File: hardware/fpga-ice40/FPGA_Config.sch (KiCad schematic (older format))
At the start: 8 parts, among them U1 iCE40HX4K-TQ144, U10 SN74LVC1G08DBVR, X1 ECS-2520MV-xxx-xx

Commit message: Component selection by MPN and routing cleanup
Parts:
- C44: MPN (none) -> CL10B104KB8NNNC
- U1: MPN (none) -> iCE40HX4K-TQ144; manf# iCE40HX4K-TQ144 -> (none)
- U10: value SN74LVC1G08DBVR -> MC74HC1G08DTT1G; MPN (none) -> MC74HC1G08DTT1G
- X1: value ECS-2520MV-xxx-xx -> 50MHz; MPN (none) -> ECS-2520MV-500-BN-TR
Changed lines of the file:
@@
 F 2 "Package_QFP:TQFP-144_20x20mm_P0.5mm" H 4300 3500 60  0001 L CNN
 F 3 "https://www.mouser.com/datasheet/2/225/FPGA-DS-02029-3-5-iCE40-LP-HX-Family-Data-Sheet-1022803.pdf" H 4300 3300 60  0001 L CNN
-F 4 "iCE40HX4K-TQ144" H 4300 3400 60  0001 L CNN "manf#"
+F 4 "" H 4300 3400 60  0001 L CNN "manf#"
+F 5 "iCE40HX4K-TQ144" H 4100 3450 50  0001 C CNN "MPN"
 	5    4100 3450
 	-1   0    0    -1
@@
 F 2 "Package_QFP:TQFP-144_20x20mm_P0.5mm" H 4300 4850 60  0001 L CNN
 F 3 "https://www.mouser.com/datasheet/2/225/FPGA-DS-02029-3-5-iCE40-LP-HX-Family-Data-Sheet-1022803.pdf" H 4300 4650 60  0001 L CNN
-F 4 "iCE40HX4K-TQ144" H 4300 4750 60  0001 L CNN "manf#"
+F 4 "" H 4300 4750 60  0001 L CNN "manf#"
+F 5 "iCE40HX4K-TQ144" H 4100 4800 50  0001 C CNN "MPN"
 	8    4100 4800
 	-1   0    0    -1
@@
 AR Path="/5F5B53E5/5F5C1BBC" Ref="X1"  Part="1"
 F 0 "X1" H 6450 5300 50  0000 L CNN
-F 1 "ECS-2520MV-xxx-xx" H 6850 5300 50  0000 L CNN
+F 1 "50MHz" H 6850 5300 50  0000 L CNN
 F 2 "ng_time:Oscillator_2.5x2.0" H 7200 4700 50  0001 C CNN
 F 3 "https://www.ecsxtal.com/store/pdf/ECS-2520MV.pdf" H 6575 5175 50  0001 C CNN
+F 4 "ECS-2520MV-500-BN-TR" H 6750 5050 50  0001 C CNN "MPN"
 	1    6750 5050
 	1    0    0    -1
@@
 F 2 "Capacitor_SMD:C_0603_1608Metric" H 6088 5050 50  0001 C CNN
 F 3 "~" H 6050 5200 50  0001 C CNN
+F 4 "CL10B104KB8NNNC" H 6050 5200 50  0001 C CNN "MPN"
 	1    6050 5200
 	1    0    0    -1
@@
 P 6950 3750
 F 0 "U10" H 7000 4000 50  0000 L CNN
-F 1 "SN74LVC1G08DBVR" H 7000 3900 50  0000 L CNN
+F 1 "MC74HC1G08DTT1G" H 7000 3900 50  0000 L CNN
 F 2 "Package_TO_SOT_SMD:SOT-23-5" H 6950 3750 50  0001 C CNN
 F 3 "http://www.ti.com/lit/sg/scyt129e/scyt129e.pdf" H 6950 3750 50  0001 C CNN
+F 4 "MC74HC1G08DTT1G" H 6950 3750 50  0001 C CNN "MPN"
 	1    6950 3750
 	1    0    0    -1

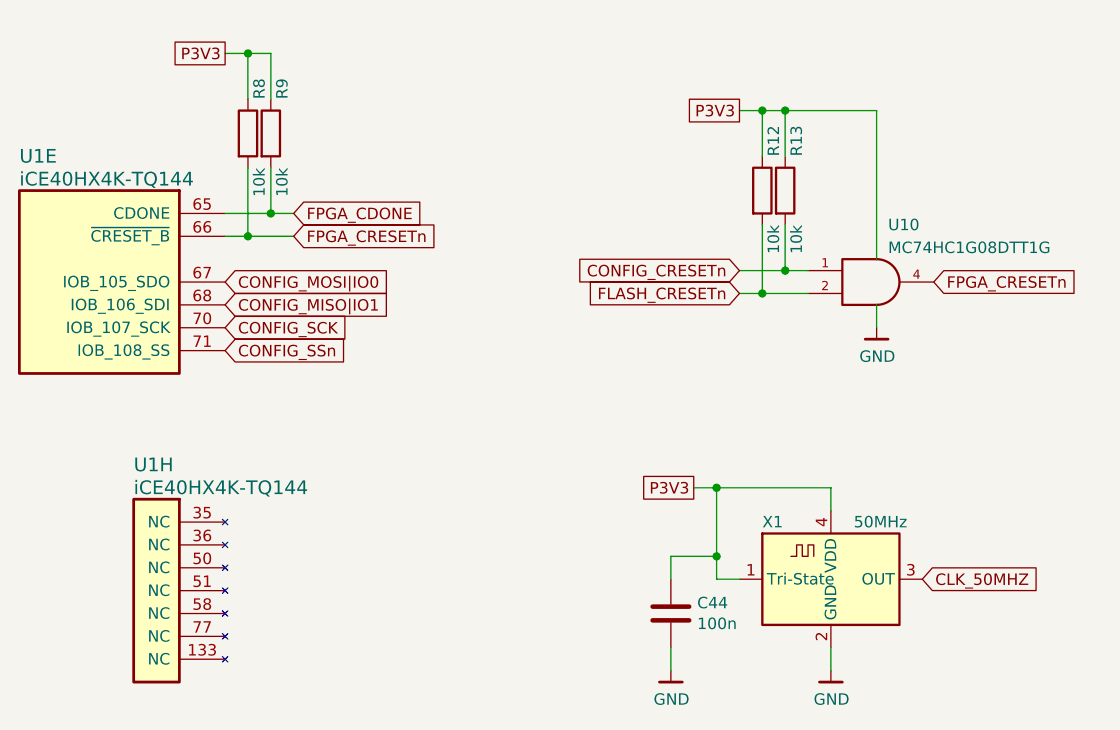
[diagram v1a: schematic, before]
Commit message: Simplify FPGA reset logic layout with resistor array
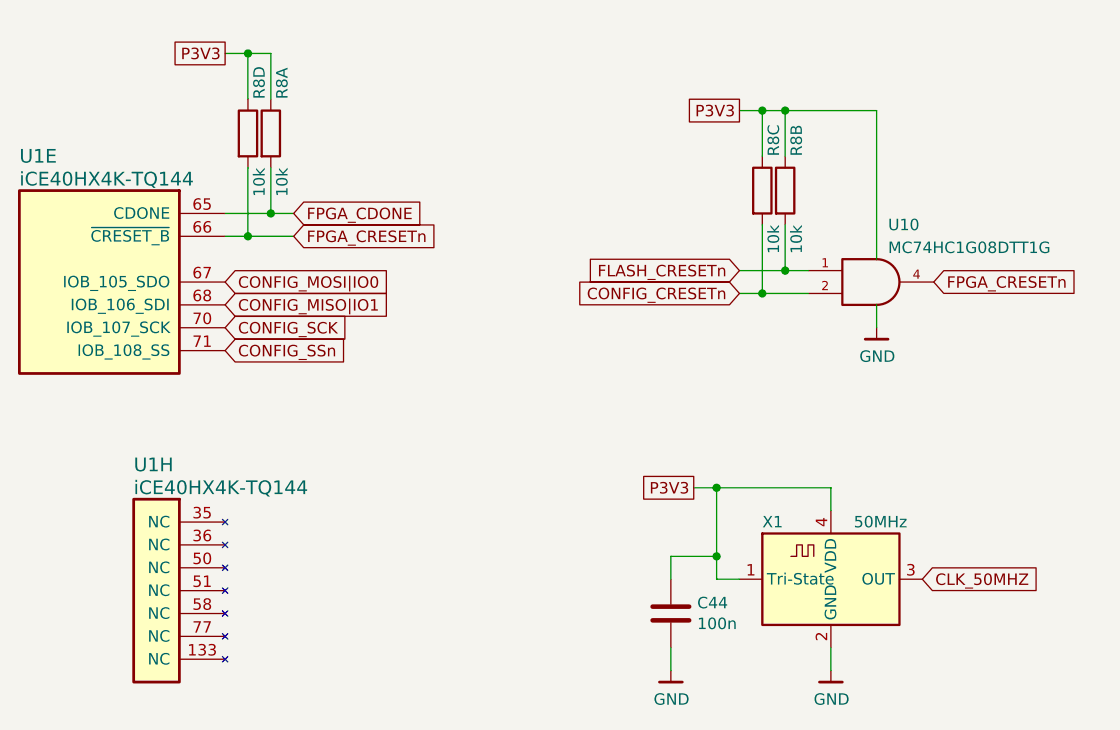
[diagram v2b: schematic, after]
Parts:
- removed R12, R13, R8, R9: 10k, Resistor_SMD:R_0603_1608Metric, symbol Device:R
- added R8: 10k, Resistor_SMD:R_Array_Convex_4x0603, symbol Device:R_Pack04_Split
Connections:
- net CONFIG_CRESETn: now also U10.2, R8.3; no longer U10.1
- net FLASH_CRESETn: now also U10.1, R8.2; no longer U10.2
- net FPGA_CDONE: now also R8.1
- net FPGA_CRESETn: now also R8.4
- net VCC: now also R8.5, R8.6, R8.7, R8.8
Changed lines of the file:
@@
 Text GLabel 4400 3550 2    50   Input ~ 0
 FPGA_CRESETn
-Wire Wire Line
-	4100 3550 4200 3550
-Wire Wire Line
-	4200 3250 4200 3550
-Connection ~ 4200 3550
-Wire Wire Line
-	4100 3450 4300 3450
-$Comp
-L Device:R R?
-U 1 1 5F5C1BA6
-P 4200 3100
-AR Path="/5F5C1BA6" Ref="R?"  Part="1"
-AR Path="/5F5B53E5/5F5C1BA6" Ref="R8"  Part="1"
-F 0 "R8" V 4250 3250 50  0000 L CNN
-F 1 "10k" V 4250 2950 50  0000 R CNN
-F 2 "Resistor_SMD:R_0603_1608Metric" V 4130 3100 50  0001 C CNN
-F 3 "~" H 4200 3100 50  0001 C CNN
-	1    4200 3100
-	1    0    0    -1
-$EndComp
-Wire Wire Line
-	4200 3550 4400 3550
-Wire Wire Line
-	4300 3450 4300 3250
-Connection ~ 4300 3450
-Wire Wire Line
-	4300 3450 4400 3450
-Wire Wire Line
-	4200 2950 4200 2750
-Wire Wire Line
-	4200 2750 4300 2750
-Wire Wire Line
-	4300 2750 4300 2950
-$Comp
-L Device:R R?
-U 1 1 5F5C1BB3
-P 4300 3100
-AR Path="/5F5C1BB3" Ref="R?"  Part="1"
-AR Path="/5F5B53E5/5F5C1BB3" Ref="R9"  Part="1"
-F 0 "R9" V 4350 3250 50  0000 L CNN
-F 1 "10k" V 4350 2950 50  0000 R CNN
-F 2 "Resistor_SMD:R_0603_1608Metric" V 4230 3100 50  0001 C CNN
-F 3 "~" H 4300 3100 50  0001 C CNN
-	1    4300 3100
-	1    0    0    -1
-$EndComp
 Text GLabel 4100 2750 0    50   UnSpc ~ 0
 P3V3
-Wire Wire Line
-	4100 2750 4200 2750
-Connection ~ 4200 2750
 $Comp
 L Oscillator:ECS-2520MV-xxx-xx X?
@@
 Wire Wire Line
 	6950 3650 6950 3000
-Wire Wire Line
-	6950 3000 6550 3000
 $Comp
 L ng_power:GND #PWR035
@@
 Wire Wire Line
 	6450 3500 6450 3800
-$Comp
-L Device:R R?
-U 1 1 5EFB670F
-P 6450 3350
-AR Path="/5EFB670F" Ref="R?"  Part="1"
-AR Path="/5F5B53E5/5EFB670F" Ref="R12"  Part="1"
-F 0 "R12" V 6500 3500 50  0000 L CNN
-F 1 "10k" V 6500 3200 50  0000 R CNN
-F 2 "Resistor_SMD:R_0603_1608Metric" V 6380 3350 50  0001 C CNN
-F 3 "~" H 6450 3350 50  0001 C CNN
-	1    6450 3350
-	1    0    0    -1
-$EndComp
 Wire Wire Line
 	6550 3700 6550 3500
-Wire Wire Line
-	6450 3200 6450 3000
-Wire Wire Line
-	6450 3000 6550 3000
-Wire Wire Line
-	6550 3000 6550 3200
-$Comp
-L Device:R R?
-U 1 1 5EFB671D
-P 6550 3350
-AR Path="/5EFB671D" Ref="R?"  Part="1"
-AR Path="/5F5B53E5/5EFB671D" Ref="R13"  Part="1"
-F 0 "R13" V 6600 3500 50  0000 L CNN
-F 1 "10k" V 6600 3200 50  0000 R CNN
-F 2 "Resistor_SMD:R_0603_1608Metric" V 6480 3350 50  0001 C CNN
-F 3 "~" H 6550 3350 50  0001 C CNN
-	1    6550 3350
-	1    0    0    -1
-$EndComp
 Text GLabel 6350 3000 0    50   UnSpc ~ 0
 P3V3
 Wire Wire Line
-	6350 3000 6450 3000
-Connection ~ 6450 3000
-Connection ~ 6550 3000
-Wire Wire Line
 	6650 3700 6550 3700
 Connection ~ 6550 3700
@@
 Wire Wire Line
 	6450 3800 6350 3800
+Text GLabel 6350 3700 0    50   Input ~ 0
+FLASH_CRESETn
 Text GLabel 6350 3800 0    50   Input ~ 0
-FLASH_CRESETn
-Text GLabel 6350 3700 0    50   Input ~ 0
 CONFIG_CRESETn
+$Comp
+L Device:R_Pack04_Split R?
+U 4 1 5EFC6F2A
+P 4200 3100
+AR Path="/5EFC6F2A" Ref="R?"  Part="1"
+AR Path="/5F90C399/5EFC6F2A" Ref="R?"  Part="1"
+AR Path="/5F5B53E5/5EFC6F2A" Ref="R8"  Part="4"
+F 0 "R8" V 4250 3250 50  0000 L CNN
+F 1 "10k" V 4250 2950 50  0000 R CNN
+F 2 "Resistor_SMD:R_Array_Convex_4x0603" V 4130 3100 50  0001 C CNN
+F 3 "~" H 4200 3100 50  0001 C CNN
+	4    4200 3100
+	1    0    0    -1
+$EndComp
+$Comp
+L Device:R_Pack04_Split R?
+U 3 1 5EFC6F23
+P 6450 3350
+AR Path="/5EFC6F23" Ref="R?"  Part="2"
+AR Path="/5F90C399/5EFC6F23" Ref="R?"  Part="2"
+AR Path="/5F5B53E5/5EFC6F23" Ref="R8"  Part="3"
+F 0 "R8" V 6500 3500 50  0000 L CNN
+F 1 "10k" V 6500 3200 50  0000 R CNN
+F 2 "Resistor_SMD:R_Array_Convex_4x0603" V 6380 3350 50  0001 C CNN
+F 3 "~" H 6450 3350 50  0001 C CNN
+	3    6450 3350
+	1    0    0    -1
+$EndComp
+$Comp
+L Device:R_Pack04_Split R?
+U 2 1 5EFC6F1C
+P 6550 3350
+AR Path="/5EFC6F1C" Ref="R?"  Part="3"
+AR Path="/5F90C399/5EFC6F1C" Ref="R?"  Part="3"
+AR Path="/5F5B53E5/5EFC6F1C" Ref="R8"  Part="2"
+F 0 "R8" V 6600 3500 50  0000 L CNN
+F 1 "10k" V 6600 3200 50  0000 R CNN
+F 2 "Resistor_SMD:R_Array_Convex_4x0603" V 6480 3350 50  0001 C CNN
+F 3 "~" H 6550 3350 50  0001 C CNN
+	2    6550 3350
+	1    0    0    -1
+$EndComp
+$Comp
+L Device:R_Pack04_Split R?
+U 1 1 5EFC6F15
+P 4300 3100
+AR Path="/5EFC6F15" Ref="R?"  Part="4"
+AR Path="/5F90C399/5EFC6F15" Ref="R?"  Part="4"
+AR Path="/5F5B53E5/5EFC6F15" Ref="R8"  Part="1"
+F 0 "R8" V 4350 3250 50  0000 L CNN
+F 1 "10k" V 4350 2950 50  0000 R CNN
+F 2 "Resistor_SMD:R_Array_Convex_4x0603" V 4230 3100 50  0001 C CNN
+F 3 "~" H 4300 3100 50  0001 C CNN
+	1    4300 3100
+	1    0    0    -1
+$EndComp
+Connection ~ 4300 3450
+Wire Wire Line
+	4300 3450 4400 3450
+Wire Wire Line
+	4100 3450 4300 3450
+Connection ~ 4200 3550
+Wire Wire Line
+	4200 3550 4400 3550
+Wire Wire Line
+	4100 3550 4200 3550
+Wire Wire Line
+	4300 3450 4300 3250
+Wire Wire Line
+	4200 3250 4200 3550
+Wire Wire Line
+	6350 3000 6450 3000
+Wire Wire Line
+	6550 3200 6550 3000
+Connection ~ 6550 3000
+Wire Wire Line
+	6550 3000 6950 3000
+Wire Wire Line
+	4200 2950 4200 2750
+Wire Wire Line
+	4300 2950 4300 2750
+Wire Wire Line
+	4100 2750 4200 2750
+Connection ~ 4200 2750
+Wire Wire Line
+	4200 2750 4300 2750
+Wire Wire Line
+	6450 3200 6450 3000
+Connection ~ 6450 3000
+Wire Wire Line
+	6450 3000 6550 3000
 $EndSCHEMATC

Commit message: Complete component selection by MPN
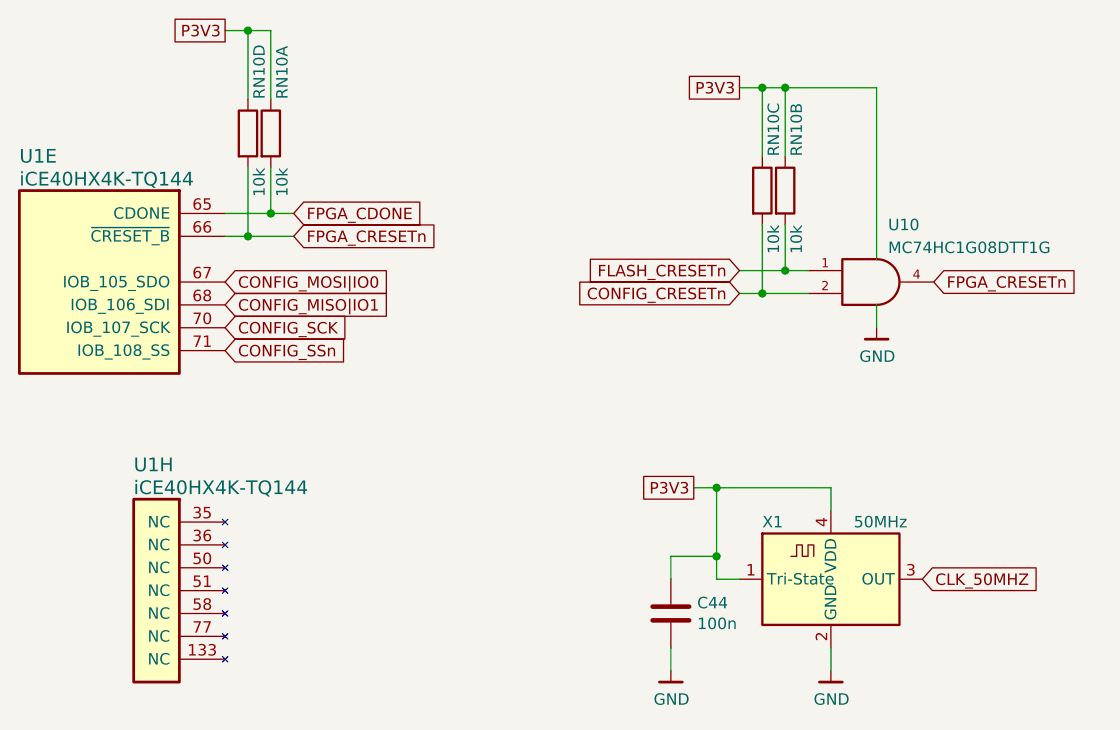
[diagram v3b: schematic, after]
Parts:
- RN10: renamed from R8; MPN (none) -> YC164-JR-0710KL
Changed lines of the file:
@@
 Text GLabel 4400 3550 2    50   Input ~ 0
 FPGA_CRESETn
-Text GLabel 4100 2750 0    50   UnSpc ~ 0
+Text GLabel 4100 2650 0    50   UnSpc ~ 0
 P3V3
 $Comp
@@
 	6950 3850 6950 3950
 Wire Wire Line
-	6950 3650 6950 3000
+	6950 3650 6950 2900
 $Comp
 L ng_power:GND #PWR035
@@
 Wire Wire Line
 	6550 3700 6550 3500
-Text GLabel 6350 3000 0    50   UnSpc ~ 0
+Text GLabel 6350 2900 0    50   UnSpc ~ 0
 P3V3
 Wire Wire Line
@@
 AR Path="/5EFC6F2A" Ref="R?"  Part="1"
 AR Path="/5F90C399/5EFC6F2A" Ref="R?"  Part="1"
-AR Path="/5F5B53E5/5EFC6F2A" Ref="R8"  Part="4"
-F 0 "R8" V 4250 3250 50  0000 L CNN
+AR Path="/5F5B53E5/5EFC6F2A" Ref="RN10"  Part="4"
+F 0 "RN10" V 4250 3250 50  0000 L CNN
 F 1 "10k" V 4250 2950 50  0000 R CNN
 F 2 "Resistor_SMD:R_Array_Convex_4x0603" V 4130 3100 50  0001 C CNN
 F 3 "~" H 4200 3100 50  0001 C CNN
+F 4 "YC164-JR-0710KL" H 4200 3100 50  0001 C CNN "MPN"
 	4    4200 3100
 	1    0    0    -1
@@
 AR Path="/5EFC6F23" Ref="R?"  Part="2"
 AR Path="/5F90C399/5EFC6F23" Ref="R?"  Part="2"
-AR Path="/5F5B53E5/5EFC6F23" Ref="R8"  Part="3"
-F 0 "R8" V 6500 3500 50  0000 L CNN
+AR Path="/5F5B53E5/5EFC6F23" Ref="RN10"  Part="3"
+F 0 "RN10" V 6500 3500 50  0000 L CNN
 F 1 "10k" V 6500 3200 50  0000 R CNN
 F 2 "Resistor_SMD:R_Array_Convex_4x0603" V 6380 3350 50  0001 C CNN
 F 3 "~" H 6450 3350 50  0001 C CNN
+F 4 "YC164-JR-0710KL" H 6450 3350 50  0001 C CNN "MPN"
 	3    6450 3350
 	1    0    0    -1
@@
 AR Path="/5EFC6F1C" Ref="R?"  Part="3"
 AR Path="/5F90C399/5EFC6F1C" Ref="R?"  Part="3"
-AR Path="/5F5B53E5/5EFC6F1C" Ref="R8"  Part="2"
-F 0 "R8" V 6600 3500 50  0000 L CNN
+AR Path="/5F5B53E5/5EFC6F1C" Ref="RN10"  Part="2"
+F 0 "RN10" V 6600 3500 50  0000 L CNN
 F 1 "10k" V 6600 3200 50  0000 R CNN
 F 2 "Resistor_SMD:R_Array_Convex_4x0603" V 6480 3350 50  0001 C CNN
 F 3 "~" H 6550 3350 50  0001 C CNN
+F 4 "YC164-JR-0710KL" H 6550 3350 50  0001 C CNN "MPN"
 	2    6550 3350
 	1    0    0    -1
@@
 AR Path="/5EFC6F15" Ref="R?"  Part="4"
 AR Path="/5F90C399/5EFC6F15" Ref="R?"  Part="4"
-AR Path="/5F5B53E5/5EFC6F15" Ref="R8"  Part="1"
-F 0 "R8" V 4350 3250 50  0000 L CNN
+AR Path="/5F5B53E5/5EFC6F15" Ref="RN10"  Part="1"
+F 0 "RN10" V 4350 3250 50  0000 L CNN
 F 1 "10k" V 4350 2950 50  0000 R CNN
 F 2 "Resistor_SMD:R_Array_Convex_4x0603" V 4230 3100 50  0001 C CNN
 F 3 "~" H 4300 3100 50  0001 C CNN
+F 4 "YC164-JR-0710KL" H 4300 3100 50  0001 C CNN "MPN"
 	1    4300 3100
 	1    0    0    -1
@@
 	4200 3250 4200 3550
 Wire Wire Line
-	6350 3000 6450 3000
-Wire Wire Line
-	6550 3200 6550 3000
-Connection ~ 6550 3000
-Wire Wire Line
-	6550 3000 6950 3000
-Wire Wire Line
-	4200 2950 4200 2750
-Wire Wire Line
-	4300 2950 4300 2750
-Wire Wire Line
-	4100 2750 4200 2750
-Connection ~ 4200 2750
-Wire Wire Line
-	4200 2750 4300 2750
-Wire Wire Line
-	6450 3200 6450 3000
-Connection ~ 6450 3000
-Wire Wire Line
-	6450 3000 6550 3000
+	6350 2900 6450 2900
+Wire Wire Line
+	6550 3200 6550 2900
+Connection ~ 6550 2900
+Wire Wire Line
+	6550 2900 6950 2900
+Wire Wire Line
+	4200 2950 4200 2650
+Wire Wire Line
+	4300 2950 4300 2650
+Wire Wire Line
+	4100 2650 4200 2650
+Connection ~ 4200 2650
+Wire Wire Line
+	4200 2650 4300 2650
+Wire Wire Line
+	6450 3200 6450 2900
+Connection ~ 6450 2900
+Wire Wire Line
+	6450 2900 6550 2900
 $EndSCHEMATC

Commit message: Completed verification of all pins for all symbols
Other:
- moved on the sheet: C44
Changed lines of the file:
@@
 F 1 "50MHz" H 6850 5300 50  0000 L CNN
 F 2 "ng_time:Oscillator_2.5x2.0" H 7200 4700 50  0001 C CNN
-F 3 "https://www.ecsxtal.com/store/pdf/ECS-2520MV.pdf" H 6575 5175 50  0001 C CNN
+F 3 "https://ecsxtal.com/store/pdf/ECS-2520MV.pdf" H 6575 5175 50  0001 C CNN
 F 4 "ECS-2520MV-500-BN-TR" H 6750 5050 50  0001 C CNN "MPN"
 	1    6750 5050
@@
 	1    0    0    -1
 $EndComp
-Text GLabel 6150 4650 0    50   UnSpc ~ 0
+Text GLabel 5950 4650 0    50   UnSpc ~ 0
 P3V3
 Wire Wire Line
 	6350 5050 6250 5050
 Wire Wire Line
-	6250 5050 6250 4950
-Wire Wire Line
 	6250 4650 6750 4650
 Wire Wire Line
 	6750 4650 6750 4750
-Wire Wire Line
-	6150 4650 6250 4650
 Wire Wire Line
 	6750 5450 6750 5350
@@
 CLK_50MHZ
 $Comp
-L Device:C C?
-U 1 1 5F5C1BD0
-P 6050 5200
-AR Path="/5F5C1BD0" Ref="C?"  Part="1"
-AR Path="/5F5B53E5/5F5C1BD0" Ref="C44"  Part="1"
-F 0 "C44" H 6165 5246 50  0000 L CNN
-F 1 "100n" H 6165 5155 50  0000 L CNN
-F 2 "Capacitor_SMD:C_0603_1608Metric" H 6088 5050 50  0001 C CNN
-F 3 "~" H 6050 5200 50  0001 C CNN
-F 4 "CL10B104KB8NNNC" H 6050 5200 50  0001 C CNN "MPN"
-	1    6050 5200
-	1    0    0    -1
-$EndComp
-$Comp
 L ng_power:GND #PWR?
 U 1 1 5F5C1BD6
-P 6050 5450
+P 6050 5150
 AR Path="/5F5C1BD6" Ref="#PWR?"  Part="1"
 AR Path="/5F5B53E5/5F5C1BD6" Ref="#PWR031"  Part="1"
-F 0 "#PWR031" H 6050 5200 50  0001 C CNN
-F 1 "GND" H 6053 5324 50  0000 C CNN
-F 2 "" H 5950 5100 50  0001 C CNN
-F 3 "" H 6050 5450 50  0001 C CNN
-	1    6050 5450
-	1    0    0    -1
-$EndComp
-Wire Wire Line
-	6050 5450 6050 5350
-Wire Wire Line
-	6050 5050 6050 4950
-Wire Wire Line
-	6050 4950 6250 4950
-Connection ~ 6250 4950
-Wire Wire Line
-	6250 4950 6250 4650
+F 0 "#PWR031" H 6050 4900 50  0001 C CNN
+F 1 "GND" H 6053 5024 50  0000 C CNN
+F 2 "" H 5950 4800 50  0001 C CNN
+F 3 "" H 6050 5150 50  0001 C CNN
+	1    6050 5150
+	1    0    0    -1
+$EndComp
+Wire Wire Line
+	6050 5150 6050 5050
 Connection ~ 6250 4650
 $Comp
@@
 F 1 "MC74HC1G08DTT1G" H 7000 3900 50  0000 L CNN
 F 2 "Package_TO_SOT_SMD:SOT-23-5" H 6950 3750 50  0001 C CNN
-F 3 "http://www.ti.com/lit/sg/scyt129e/scyt129e.pdf" H 6950 3750 50  0001 C CNN
+F 3 "https://www.onsemi.com/pub/Collateral/MC74HC1G08-D.PDF" H 6950 3750 50  0001 C CNN
 F 4 "MC74HC1G08DTT1G" H 6950 3750 50  0001 C CNN "MPN"
 	1    6950 3750
@@
 Wire Wire Line
 	6450 2900 6550 2900
+Wire Wire Line
+	6250 4650 6250 5050
+Wire Wire Line
+	5950 4650 6050 4650
+Wire Wire Line
+	6050 4750 6050 4650
+Connection ~ 6050 4650
+Wire Wire Line
+	6050 4650 6250 4650
+$Comp
+L Device:C C?
+U 1 1 5F5C1BD0
+P 6050 4900
+AR Path="/5F5C1BD0" Ref="C?"  Part="1"
+AR Path="/5F5B53E5/5F5C1BD0" Ref="C44"  Part="1"
+F 0 "C44" H 5950 4950 50  0000 R CNN
+F 1 "100n" H 5950 4850 50  0000 R CNN
+F 2 "Capacitor_SMD:C_0603_1608Metric" H 6088 4750 50  0001 C CNN
+F 3 "~" H 6050 4900 50  0001 C CNN
+F 4 "CL10B104KB8NNNC" H 6050 4900 50  0001 C CNN "MPN"
+	1    6050 4900
+	1    0    0    -1
+$EndComp
 $EndSCHEMATC
